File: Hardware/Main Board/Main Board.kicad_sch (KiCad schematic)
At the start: 52 parts, among them J1 Micro_SD_Card_Det1, J2 Conn_01x06_Socket, J3 USB_C_Receptacle_USB2.0_16P, J4 Conn_01x09_Socket, SW1 SW_SPST, SW2 SW_Push, SW3 SW_Push, U1 ESP32-S3-WROOM-2, U3 TP4056-42-ESOP8, U4 TPS63060

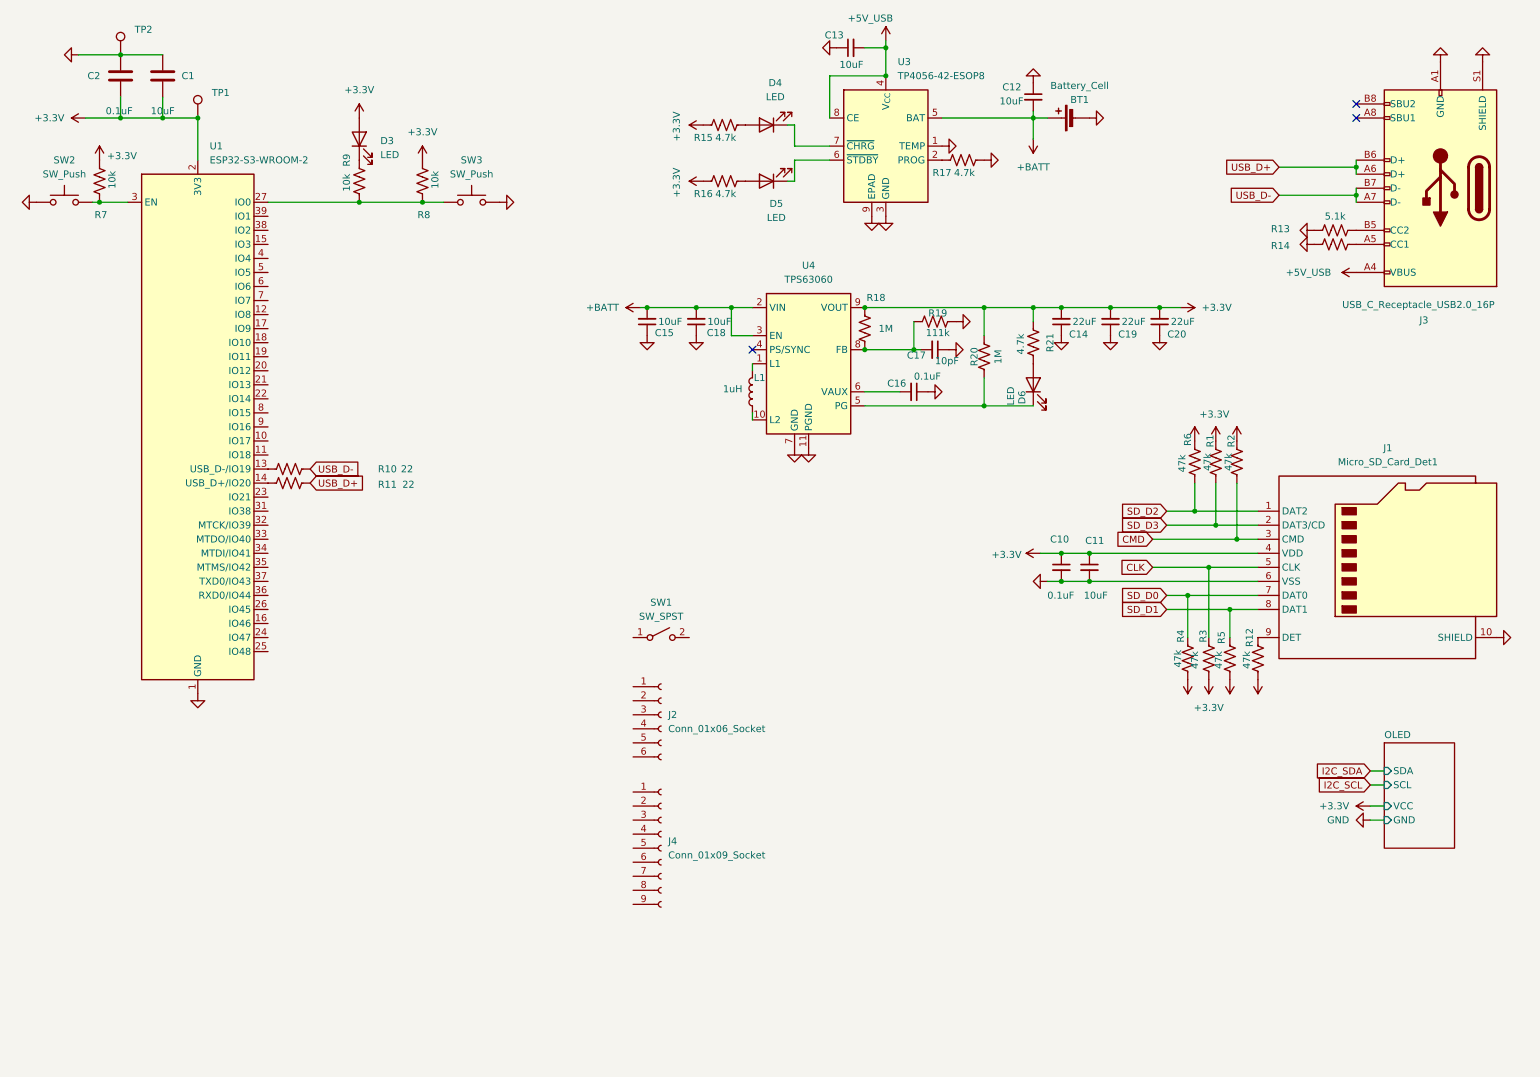
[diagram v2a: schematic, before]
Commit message: drafted entire main board schematic and assigned footprints
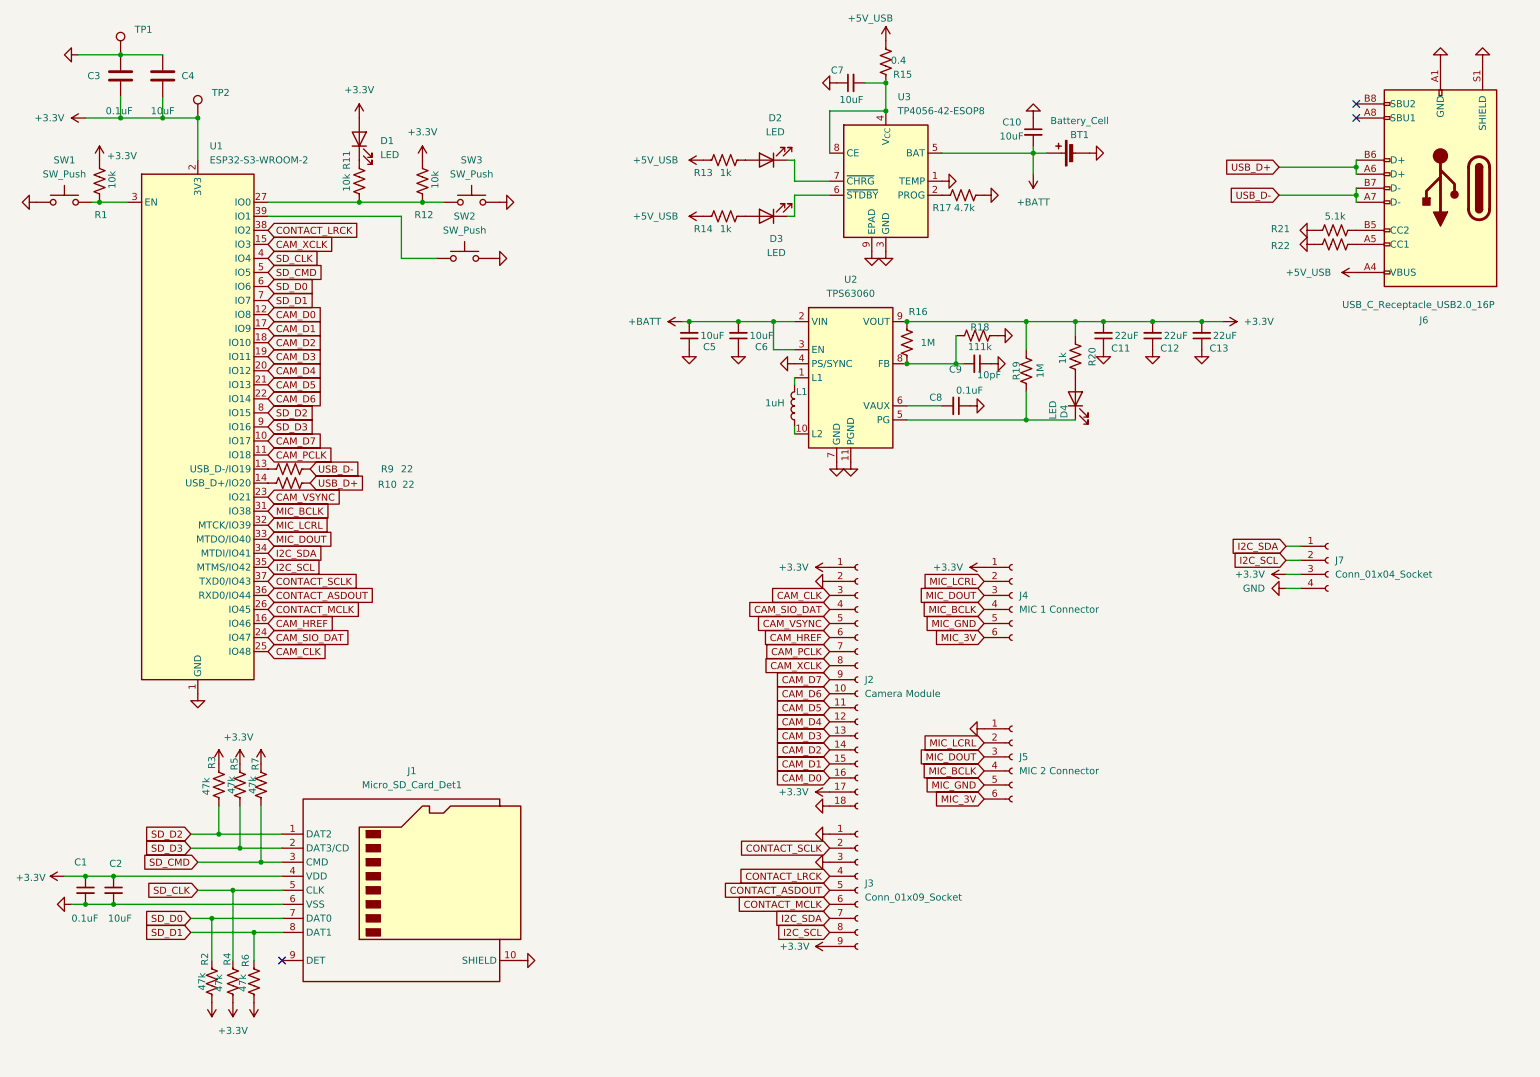
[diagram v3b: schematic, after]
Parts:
- removed R12: 47k, symbol Device:R_US
- removed SW1: SW_SPST, symbol Switch:SW_SPST
- added J2: Camera Module, Connector_PinHeader_2.54mm:PinHeader_2x09_P2.54mm_Vertical, symbol Connector:Conn_01x18_Socket
- added J5: MIC 2 Connector, Connector_PinHeader_2.54mm:PinHeader_1x06_P2.54mm_Vertical, symbol Connector:Conn_01x06_Socket
- added J7: Conn_01x04_Socket, Connector_PinHeader_2.54mm:PinHeader_1x04_P2.54mm_Vertical, symbol Connector:Conn_01x04_Socket
- added R15: 0.4, Resistor_SMD:R_0201_0603Metric, symbol Device:R_US
- added SW2: SW_Push, Button_Switch_SMD:SW_SPST_PTS645, symbol Switch:SW_Push
- BT1: footprint (none) -> Connector_PinHeader_2.54mm:PinHeader_1x02_P2.54mm_Vertical
- C1: renamed from C10; footprint (none) -> Capacitor_SMD:C_01005_0402Metric
- C10: renamed from C12; footprint (none) -> Capacitor_SMD:C_01005_0402Metric
- C11: renamed from C14; footprint (none) -> Capacitor_SMD:C_01005_0402Metric
- C12: renamed from C19; footprint (none) -> Capacitor_SMD:C_01005_0402Metric
- C13: renamed from C20; footprint (none) -> Capacitor_SMD:C_01005_0402Metric
- C2: renamed from C11; footprint (none) -> Capacitor_SMD:C_01005_0402Metric
- C3: renamed from C2; footprint (none) -> Capacitor_SMD:C_01005_0402Metric
- C4: renamed from C1; footprint (none) -> Capacitor_SMD:C_01005_0402Metric
- C5: renamed from C15; footprint (none) -> Capacitor_SMD:C_01005_0402Metric
- C6: renamed from C18; footprint (none) -> Capacitor_SMD:C_01005_0402Metric
- C7: renamed from C13; footprint (none) -> Capacitor_SMD:C_01005_0402Metric
- C8: renamed from C16; footprint (none) -> Capacitor_SMD:C_01005_0402Metric
- C9: renamed from C17; footprint (none) -> Capacitor_SMD:C_01005_0402Metric
- D1: renamed from D3; footprint (none) -> LED_SMD:LED_0201_0603Metric
- D2: renamed from D4; footprint (none) -> LED_SMD:LED_0201_0603Metric
- D3: renamed from D5; footprint (none) -> LED_SMD:LED_0201_0603Metric
- D4: renamed from D6; footprint (none) -> LED_SMD:LED_0201_0603Metric
- J1: footprint (none) -> Connector_Card:microSD_HC_Molex_104031-0811
- J3: renamed from J4; footprint (none) -> Connector_PinHeader_2.54mm:PinHeader_1x09_P2.54mm_Vertical
- J4: renamed from J2; value Conn_01x06_Socket -> MIC 1 Connector; footprint (none) -> Connector_PinHeader_2.54mm:PinHeader_1x06_P2.54mm_Vertical
- J6: renamed from J3; footprint (none) -> Connector_USB:USB_C_Receptacle_HRO_TYPE-C-31-M-12
- L1: footprint (none) -> Inductor_SMD:L_0603_1608Metric
- R1: renamed from R7; footprint (none) -> Resistor_SMD:R_0201_0603Metric
- R10: renamed from R11; footprint (none) -> Resistor_SMD:R_0201_0603Metric
- R11: renamed from R9; footprint (none) -> Resistor_SMD:R_0201_0603Metric
- R12: renamed from R8; footprint (none) -> Resistor_SMD:R_0201_0603Metric
- R13: renamed from R15; value 4.7k -> 1k; footprint (none) -> Resistor_SMD:R_0201_0603Metric
- R14: renamed from R16; value 4.7k -> 1k; footprint (none) -> Resistor_SMD:R_0201_0603Metric
- R16: renamed from R18; footprint (none) -> Resistor_SMD:R_0201_0603Metric
- R17: footprint (none) -> Resistor_SMD:R_0201_0603Metric
- R18: renamed from R19; footprint (none) -> Resistor_SMD:R_0201_0603Metric
- R19: renamed from R20; footprint (none) -> Resistor_SMD:R_0201_0603Metric
- R2: renamed from R4; footprint (none) -> Resistor_SMD:R_0201_0603Metric
- R20: renamed from R21; value 4.7k -> 1k; footprint (none) -> Resistor_SMD:R_0201_0603Metric
- R21: renamed from R13; footprint (none) -> Resistor_SMD:R_0201_0603Metric
- R22: renamed from R14; footprint (none) -> Resistor_SMD:R_0201_0603Metric
- R3: renamed from R6; footprint (none) -> Resistor_SMD:R_0201_0603Metric
- R4: renamed from R3; footprint (none) -> Resistor_SMD:R_0201_0603Metric
- R5: renamed from R1; footprint (none) -> Resistor_SMD:R_0201_0603Metric
- R6: renamed from R5; footprint (none) -> Resistor_SMD:R_0201_0603Metric
- R7: renamed from R2; footprint (none) -> Resistor_SMD:R_0201_0603Metric
- R9: renamed from R10; footprint (none) -> Resistor_SMD:R_0201_0603Metric
- SW1: renamed from SW2; footprint (none) -> Button_Switch_SMD:SW_SPST_PTS645
- SW3: footprint (none) -> Button_Switch_SMD:SW_SPST_PTS645
- TP1: renamed from TP2; footprint (none) -> TestPoint:TestPoint_Pad_D1.0mm
- TP2: renamed from TP1; footprint (none) -> TestPoint:TestPoint_Pad_D1.0mm
- renumbered U4 to U2
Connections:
- net CLK is gone; now on net SD_CLK: J1.5 (CLK), R4.2
- net CMD is gone; now on net SD_CMD: J1.3 (CMD), R7.1
- net +3.3V: now also J3.9 (Pin_9), J4.1 (Pin_1), J2.1 (Pin_1), J2.17 (Pin_17), J7.3 (Pin_3); no longer R13.2, R14.2
- net +5V_USB: now also R13.2, R14.2, R15.1; no longer C7.2, U3.4 (V_{CC}), U3.8 (CE)
- net GND: now also J3.1 (Pin_1), J3.3 (Pin_3), U2.4 (PS/SYNC), J2.18 (Pin_18), J2.2 (Pin_2), J5.1 (Pin_1), J7.4 (Pin_4), SW2.2
- net I2C_SCL: now also J3.8 (Pin_8), U1.35 (MTMS/IO42), J7.2 (Pin_2)
- net I2C_SDA: now also J3.7 (Pin_7), U1.34 (MTDI/IO41), J7.1 (Pin_1)
- net SD_D0: now also U1.6 (IO6)
- net SD_D1: now also U1.7 (IO7)
- net SD_D2: now also U1.8 (IO15)
- net SD_D3: now also U1.9 (IO16)
- net CAM_D7: now reaches U1.10 (IO17)
- net CAM_D7: now also J2.9 (Pin_9)
- net CAM_PCLK: now reaches U1.11 (IO18)
- net CAM_PCLK: now also J2.7 (Pin_7)
- net CAM_D0: now reaches U1.12 (IO8)
- net CAM_D0: now also J2.16 (Pin_16)
- net CAM_XCLK: now reaches U1.15 (IO3)
- net CAM_XCLK: now also J2.8 (Pin_8)
- net CAM_HREF: now reaches U1.16 (IO46)
- net CAM_HREF: now also J2.6 (Pin_6)
- net CAM_D1: now reaches U1.17 (IO9)
- net CAM_D1: now also J2.15 (Pin_15)
- net CAM_D2: now reaches U1.18 (IO10)
- net CAM_D2: now also J2.14 (Pin_14)
- net CAM_D3: now reaches U1.19 (IO11)
- net CAM_D3: now also J2.13 (Pin_13)
- net CAM_D4: now reaches U1.20 (IO12)
- net CAM_D4: now also J2.12 (Pin_12)
- net CAM_D5: now reaches U1.21 (IO13)
- net CAM_D5: now also J2.11 (Pin_11)
- net CAM_D6: now reaches U1.22 (IO14)
- net CAM_D6: now also J2.10 (Pin_10)
- net CAM_VSYNC: now reaches U1.23 (IO21)
- net CAM_VSYNC: now also J2.5 (Pin_5)
- net CAM_SIO_DAT: now reaches U1.24 (IO47)
- net CAM_SIO_DAT: now also J2.4 (Pin_4)
- net CAM_CLK: now reaches U1.25 (IO48)
- net CAM_CLK: now also J2.3 (Pin_3)
- net CONTACT_MCLK: now reaches U1.26 (IO45)
- net CONTACT_MCLK: now also J3.6 (Pin_6)
- net MIC_BCLK: now reaches U1.31 (IO38)
- net MIC_BCLK: now also J4.4 (Pin_4), J5.4 (Pin_4)
- net MIC_LCRL: now reaches U1.32 (MTCK/IO39)
- net MIC_LCRL: now also J4.2 (Pin_2), J5.2 (Pin_2)
- net MIC_DOUT: now reaches U1.33 (MTDO/IO40)
- net MIC_DOUT: now also J4.3 (Pin_3), J5.3 (Pin_3)
- net CONTACT_ASDOUT: now reaches U1.36 (RXD0/IO44)
- net CONTACT_ASDOUT: now also J3.5 (Pin_5)
- net CONTACT_SCLK: now reaches U1.37 (TXD0/IO43)
- net CONTACT_SCLK: now also J3.2 (Pin_2)
- net CONTACT_LRCK: now reaches U1.38 (IO2)
- net CONTACT_LRCK: now also J3.4 (Pin_4)
- net at U1.39 (IO1): now also SW2.1
- net SD_CLK: now reaches U1.4 (IO4)
- net SD_CMD: now reaches U1.5 (IO5)
- net MIC_GND: now reaches J4.5 (Pin_5)
- net MIC_GND: now also J5.5 (Pin_5)
- net MIC_3V: now reaches J4.6 (Pin_6)
- net MIC_3V: now also J5.6 (Pin_6)
- new net: C7.2, R15.2, U3.4 (V_{CC}), U3.8 (CE)
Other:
- removed sheet OLED
- moved on the sheet: BT1, C1, C10, C11, C12, C13, C2, C5, C6, C7, C8, C9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

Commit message: drafted main board layout
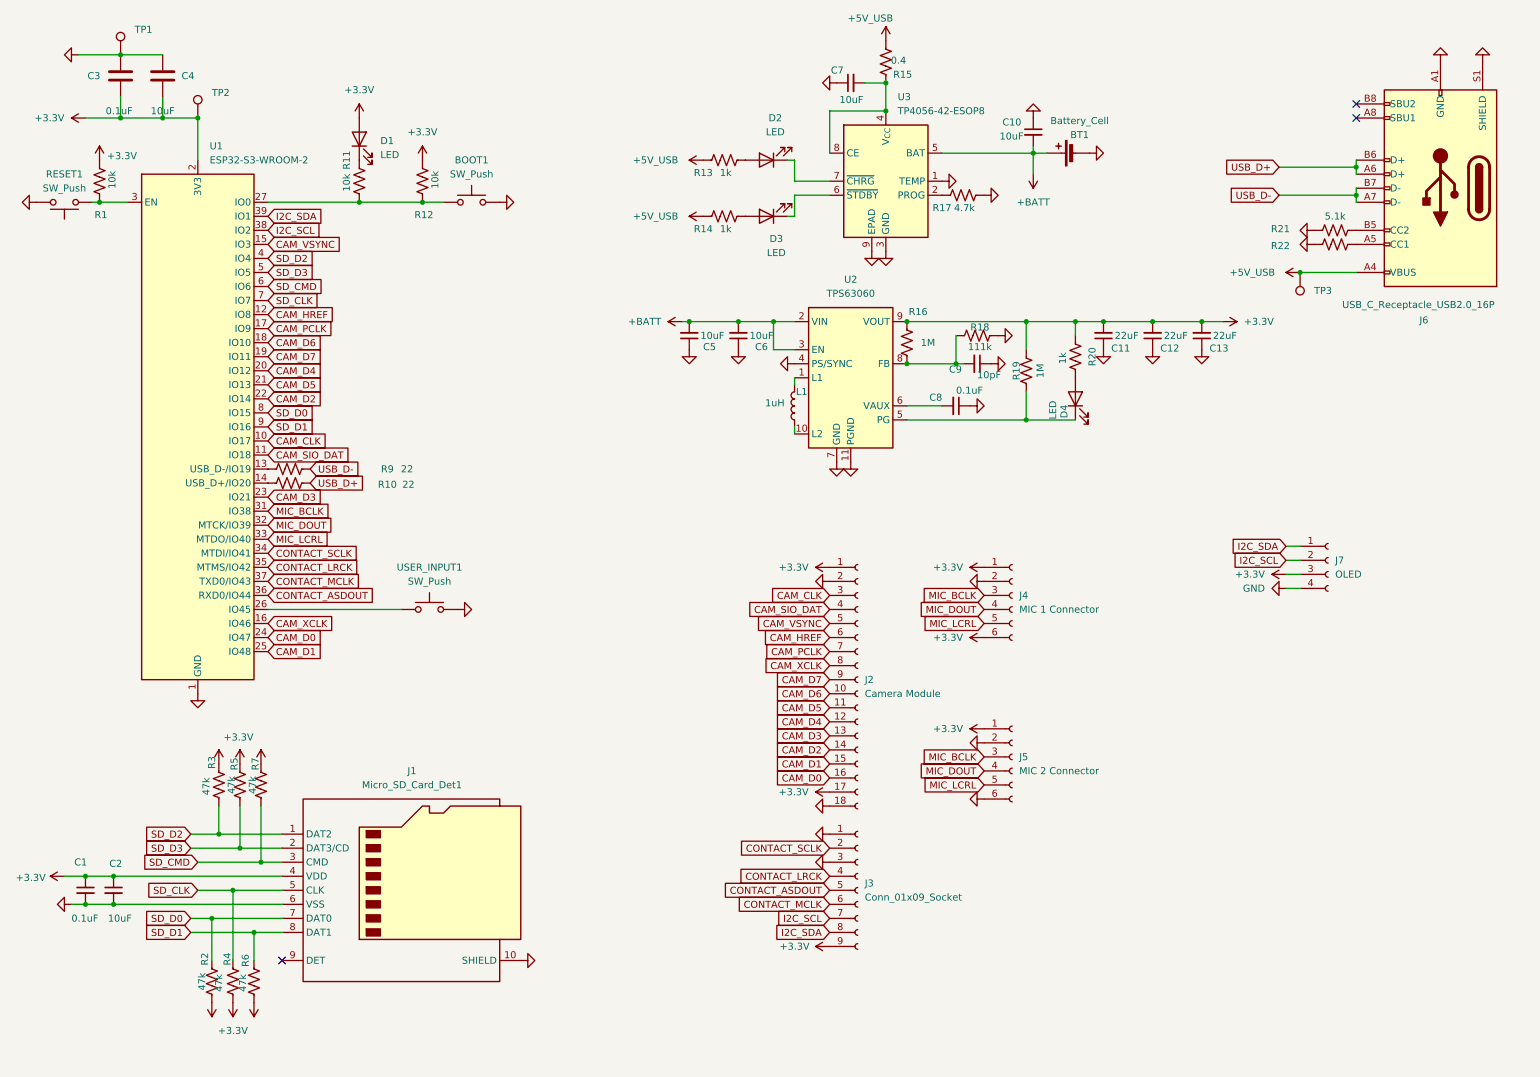
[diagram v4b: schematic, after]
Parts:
- added TP3: TestPoint, TestPoint:TestPoint_Pad_D1.0mm, symbol Connector:TestPoint
- BOOT1: renamed from SW3; footprint Button_Switch_SMD:SW_SPST_PTS645 -> Button_Switch_SMD:SW_SPST_EVQP7A
- BT1: footprint Connector_PinHeader_2.54mm:PinHeader_1x02_P2.54mm_Vertical -> Connector_JST:JST_GH_SM02B-GHS-TB_1x02-1MP_P1.25mm_Horizontal
- J3: footprint Connector_PinHeader_2.54mm:PinHeader_1x09_P2.54mm_Vertical -> Connector_JST:JST_GH_SM09B-GHS-TB_1x09-1MP_P1.25mm_Horizontal
- J4, J5: footprint Connector_PinHeader_2.54mm:PinHeader_1x06_P2.54mm_Vertical -> Connector_JST:JST_GH_SM06B-GHS-TB_1x06-1MP_P1.25mm_Horizontal
- J7: value Conn_01x04_Socket -> OLED
- RESET1: renamed from SW1; footprint Button_Switch_SMD:SW_SPST_PTS645 -> Button_Switch_SMD:SW_SPST_EVQP7A
- renumbered SW2 to USER_INPUT1
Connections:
- net MIC_GND is gone; now on net MIC_LCRL: J4.5 (Pin_5), J5.5 (Pin_5)
- net +3.3V: now also J4.6 (Pin_6), J5.1 (Pin_1)
- net +5V_USB: now also TP3.1
- net CAM_CLK: now also U1.10 (IO17); no longer U1.25 (IO48)
- net CAM_D0: now also U1.24 (IO47); no longer U1.12 (IO8)
- net CAM_D1: now also U1.25 (IO48); no longer U1.17 (IO9)
- net CAM_D2: now also U1.22 (IO14); no longer U1.18 (IO10)
- net CAM_D3: now also U1.23 (IO21); no longer U1.19 (IO11)
- net CAM_D6: now also U1.18 (IO10); no longer U1.22 (IO14)
- net CAM_D7: now also U1.19 (IO11); no longer U1.10 (IO17)
- net CAM_HREF: now also U1.12 (IO8); no longer U1.16 (IO46)
- net CAM_PCLK: now also U1.17 (IO9); no longer U1.11 (IO18)
- net CAM_SIO_DAT: now also U1.11 (IO18); no longer U1.24 (IO47)
- net CAM_VSYNC: now also U1.15 (IO3); no longer U1.23 (IO21)
- net CAM_XCLK: now also U1.16 (IO46); no longer U1.15 (IO3)
- net CONTACT_LRCK: now also U1.35 (MTMS/IO42); no longer U1.38 (IO2)
- net CONTACT_MCLK: now also U1.37 (TXD0/IO43); no longer U1.26 (IO45)
- net CONTACT_SCLK: now also U1.34 (MTDI/IO41); no longer U1.37 (TXD0/IO43)
- net GND: now also J4.2 (Pin_2), J5.2 (Pin_2), J5.6 (Pin_6), RESET1.2; no longer J5.1 (Pin_1), RESET1.1
- net I2C_SCL: now also J3.7 (Pin_7), U1.38 (IO2); no longer J3.8 (Pin_8), U1.35 (MTMS/IO42)
- net I2C_SDA: now also J3.8 (Pin_8), U1.39 (IO1); no longer J3.7 (Pin_7), U1.34 (MTDI/IO41)
- net MIC_BCLK: now also J4.3 (Pin_3), J5.3 (Pin_3); no longer J4.4 (Pin_4), J5.4 (Pin_4)
- net MIC_DOUT: now also J4.4 (Pin_4), J5.4 (Pin_4), U1.32 (MTCK/IO39); no longer J4.3 (Pin_3), J5.3 (Pin_3), U1.33 (MTDO/IO40)
- net MIC_LCRL: now also U1.33 (MTDO/IO40); no longer J4.2 (Pin_2), J5.2 (Pin_2), U1.32 (MTCK/IO39)
- net SD_CLK: now also U1.7 (IO7); no longer U1.4 (IO4)
- net SD_CMD: now also U1.6 (IO6); no longer U1.5 (IO5)
- net SD_D0: now also U1.8 (IO15); no longer U1.6 (IO6)
- net SD_D1: now also U1.9 (IO16); no longer U1.7 (IO7)
- net SD_D2: now also U1.4 (IO4); no longer U1.8 (IO15)
- net SD_D3: now also U1.5 (IO5); no longer U1.9 (IO16)
- net at USER_INPUT1.1: now also U1.26 (IO45); no longer U1.39 (IO1)
- net at R1.2, U1.3 (EN): now also RESET1.1; no longer RESET1.2
- removed net MIC_3V: J4.6 (Pin_6), J5.6 (Pin_6)
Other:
- moved on the sheet: RESET1, USER_INPUT1
